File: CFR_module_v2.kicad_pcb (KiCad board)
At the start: 4 copper layers, 80.9 x 70.9 mm, 67 parts, among them J3 Conn_01x02, J4 Conn_01x02, J5 Conn_01x02, Q1 NPN

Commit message: placement des empreintes début
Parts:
- moved D11 37.2 mm to (27.0, 138.7)
- moved R5 37.2 mm to (27.0, 143.3)
- moved C2 36.5 mm to (58.0, 127.5)
- moved ALM1 35.1 mm to (114.0, 130.5)
- moved ALM2 35.1 mm to (97.0, 130.0)
- moved C3 34.2 mm to (56.5, 146.5)
- moved JP1 9.70 mm to (54.5, 65.6), turned to -90 degrees
- moved JP2 7.19 mm to (54.5, 62.0), turned to -90 degrees
- moved R6 1.28 mm to (126.0, 54.5)
- moved C4 0.90 mm to (51.5, 71.0)

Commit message: tout connecté
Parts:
- removed ALM1, ALM2, ALM3: Conn_01x02, Connector_AMASS:AMASS_XT30U-F_1x02_P5.0mm_Vertical
- removed D10, D11, D12: D_Schottky, Diode_SMD:D_SOD-123
- added ALM0: Conn_02x03_Odd_Even, Connector_Molex:Molex_Mini-Fit_Jr_5569-06A2_2x03_P4.20mm_Horizontal, F.Cu at (110.3, 136.8)
- added JP15: Jumper_3_Bridged12, Connector_PinHeader_2.54mm:PinHeader_1x03_P2.54mm_Vertical, F.Cu at (82.8, 86.5)
- added JP16: Jumper_3_Bridged12, Connector_PinHeader_2.54mm:PinHeader_1x03_P2.54mm_Vertical, F.Cu at (82.8, 83.0)
- added JP17: Jumper_3_Bridged12, Connector_PinHeader_2.54mm:PinHeader_1x03_P2.54mm_Vertical, F.Cu at (82.8, 108.5)
- added JP18: Jumper_3_Bridged12, Connector_PinHeader_2.54mm:PinHeader_1x03_P2.54mm_Vertical, F.Cu at (82.8, 105.0)
- added JP19: Jumper_3_Bridged12, Connector_PinHeader_2.54mm:PinHeader_1x03_P2.54mm_Vertical, F.Cu at (82.8, 130.5)
- added JP20: Jumper_3_Bridged12, Connector_PinHeader_2.54mm:PinHeader_1x03_P2.54mm_Vertical, F.Cu at (82.8, 127.0)
- added R4: 10k, Resistor_SMD:R_0805_2012Metric_Pad1.20x1.40mm_HandSolder, B.Cu at (104.5, 87.0)
- BAU1, DBG1, J3, J4, J5: footprint Connector_PinHeader_2.54mm:PinHeader_1x02_P2.54mm_Vertical -> Connector_JST:JST_XH_S2B-XH-A_1x02_P2.50mm_Horizontal
- IO1, IO2: footprint Connector_JST:JST_PH_B4B-PH-K_1x04_P2.00mm_Vertical -> Connector_JST:JST_XH_S4B-XH-A_1x04_P2.50mm_Horizontal
- IO3, IO4, IO5: footprint Connector_JST:JST_PH_B3B-PH-K_1x03_P2.00mm_Vertical -> Connector_JST:JST_XH_S3B-XH-A_1x03_P2.50mm_Horizontal
- MOT1, MOT2, MOT3: value Conn_01x04 -> Conn_02x04_Odd_Even; footprint Connector_PinHeader_2.54mm:PinHeader_1x04_P2.54mm_Vertical -> Connector_PinHeader_2.54mm:PinHeader_2x04_P2.54mm_Horizontal
- R3: value 10k -> 1k
- R5: renamed from R4; value 1k -> 10k
- R6: renamed from R5; value 1k -> 10k
- R7: renamed from R6; value 1k -> 10k
- moved MOT3 128.3 mm to (75.2, 125.6), turned to 180 degrees
- moved C6 123.4 mm to (72.0, 131.1), turned to 180 degrees
- moved DR3 118.1 mm to (78.5, 115.5), turned to 0 degrees
- moved R2 103.5 mm to (123.0, 138.5), turned to 180 degrees
- moved JP5 102.0 mm to (82.8, 122.5), turned to 90 degrees
- moved JP6 98.5 mm to (82.8, 119.0), turned to 90 degrees
- moved BAU1 88.2 mm to (125.0, 141.6), turned to 0 degrees
- moved D9 77.5 mm to (95.5, 120.5), turned to 90 degrees
- moved R6 66.1 mm to (86.0, 113.5), turned to 90 degrees
- moved R7 64.8 mm to (113.0, 118.0), turned to 180 degrees
- moved D8 62.3 mm to (94.5, 113.0)
- moved IO2 58.2 mm to (127.6, 119.5)
- moved D2 58.1 mm to (124.9, 117.5)
- moved IO3 58.1 mm to (127.6, 105.8), turned to 90 degrees
- moved JP8 57.9 mm to (122.3, 115.5)
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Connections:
- net GP0 renamed Net-(DBG1-Pin_2)
- net GP1 renamed Net-(DBG1-Pin_1)
- net GP10 renamed M1_EN_GPIO
- net GP11 renamed M2_IA1_DIR
- net GP12 renamed M2_IA2_STEP
- net GP13 renamed M2_IB1
- net GP14 renamed M2_IB2
- net GP15 renamed M2_EN_GPIO
- net GP16 renamed IO_B1
- net GP17 renamed IO_B2
- net GP18 renamed M3_IA1_DIR
- net GP19 renamed M3_IA2_STEP
- net GP2 renamed IO_A1
- net GP20 renamed M3_IB1
- net GP21 renamed M3_IB2
- net GP22 renamed M3_EN_GPIO
- net GP26_A0 renamed IO_C
- net GP27_A1 renamed IO_D
- net GP28_A2 renamed IO_E
- net GP3 renamed IO_A2
- net GP4 renamed Net-(PiPico0-GPIO4)
- net GP5 renamed M_UART
- net GP6 renamed M1_IA1_DIR
- net GP7 renamed M1_IA2_STEP
- net GP8 renamed M1_IB1
- net GP9 renamed M1_IB2
- D6 pad 2: +5V_Pico -> +5V
- DR1 pad 10: GND -> M1_MS1
- DR1 pad 11: GND -> M1_MS2
- DR2 pad 10: GND -> M2_MS1
- DR2 pad 11: +3V3_Pico -> M2_MS2
- DR3 pad 10: +3V3_Pico -> M3_MS1
- DR3 pad 11: GND -> M3_MS2
- F1 pad 1: +BATT -> VBatt_in
- F1 pad 2: Net-(ALM1-Pin_2) -> +BATT
- F2 pad 2: Net-(ALM2-Pin_2) -> V0_in
- F3 pad 2: Net-(ALM3-Pin_2) -> 5V_in
- JP12 pad 3: +5V_Pico -> +5V
- MOT1 pad 2: Net-(DR1-OA2) -> GND
- MOT1 pad 3: Net-(DR1-OB2) -> Net-(DR1-OA2)
- MOT1 pad 4: Net-(DR1-OB1) -> GND
- MOT2 pad 2: Net-(DR2-OA2) -> GND
- MOT2 pad 3: Net-(DR2-OB2) -> Net-(DR2-OA2)
- MOT2 pad 4: Net-(DR2-OB1) -> GND
- MOT3 pad 2: Net-(DR3-OA2) -> GND
- MOT3 pad 3: Net-(DR3-OB2) -> Net-(DR3-OA2)
- MOT3 pad 4: Net-(DR3-OB1) -> GND
- PiPico0 pad 30: RUN -> unconnected-(PiPico0-RUN-Pad30)
- PiPico0 pad 33: AGND -> unconnected-(PiPico0-AGND-Pad33)
- PiPico0 pad 35: ADC_VREF -> unconnected-(PiPico0-ADC_VREF-Pad35)
- PiPico0 pad 37: 3V3_EN -> unconnected-(PiPico0-3V3_EN-Pad37)
- PiPico0 pad 40: VBUS -> unconnected-(PiPico0-VBUS-Pad40)
- Q1 pad 1: Net-(D7-A) -> Net-(Q1-C)
- R3 pad 2: Net-(D7-A) -> Net-(Q1-C)
- R5 pad 2: Net-(D10-A) -> M1_EN
- R6 pad 2: Net-(D11-A) -> M2_EN
- R7 pad 2: Net-(D12-A) -> M3_EN
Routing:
- net +3V3_Pico: track 0.00 -> 150.6 mm, vias 0 -> 1
- net M_UART: track 0.00 -> 82.9 mm, vias 0 -> 1
- net IO_A1: track 0.00 -> 68.0 mm, vias 0 -> 1
- net IO_A2: track 0.00 -> 64.4 mm, vias 0 -> 1
- net Net-(Q1-B): track 0.00 -> 64.1 mm, vias 0 -> 2
- net M3_IB2: track 0.00 -> 60.6 mm
- net M3_IB1: track 0.00 -> 56.1 mm
- net GND: track 0.00 -> 52.5 mm, vias 0 -> 30
- net M3_IA2_STEP: track 0.00 -> 42.6 mm
- net Net-(D7-A): track 0.00 -> 36.2 mm
- net M3_IA1_DIR: track 0.00 -> 31.2 mm
- net M3_EN: track 0.00 -> 31.1 mm
- net +5V: track 0.00 -> 30.8 mm, vias 0 -> 2
- net M1_IB1: track 0.00 -> 30.0 mm
- net Net-(DBG1-Pin_2): track 0.00 -> 29.7 mm
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- added copper zone on In2.Cu, net +5V
- added copper zone on In2.Cu, net +BATT
- added copper zone on In2.Cu, net +V0
- added copper zone on In2.Cu, net +V1
- added copper zone on In2.Cu, net +V2
- added copper zone on In1.Cu, net GND
- added copper zone on In2.Cu, net VBatt_in
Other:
- board size 80.9 x 70.9 mm -> 72.9 x 88.5 mm
- board text added: "(I2C0,UART0)"
- board text added: "+Batt"
- board text added: "10k"
- board text added: "1k"
- board text added: "EN 10 B1 8 B2 9 A1 DR 6 A2 SP 7 UART 5"
- board text added: "EN 15 B1 13 B2 14 A1-DR 11 A2-SP 12 UART 5"
- board text added: "EN 22 B1 20 B2 21 A1-DR 18 A2-SP 19 UART 5"
- board text added: "IB1"
- board text added: "IB12"
- board text added: "IO1"
- board text added: "IO2"
- board text added: "IO3"
- board text added: "IO4"
- board text added: "IO5"
- board text added: "MS1"
- board text added: "MS2"
- board text removed: "(I2C0, UART0)"
- board text removed: "(Pico)"
- board text removed: "EN: GP10 IB1: GP8 IB2: GP9 IA1-DIR: GP6 IA2-STEP: GP7 UART: GP5"
- board text removed: "EN: GP15 IB1: GP13 IB2: GP14 IA1-DIR: GP11 IA2-STEP: GP12 UART: GP5"
- board text removed: "EN: GP22 IB1: GP20 IB2: GP21 IA1-DIR: GP18 IA2-STEP: GP19 UART: GP5"
- board text removed: "RX/GP1"
- board text removed: "TX/GP0"
- board text removed: "VI"

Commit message: v2 finalisé
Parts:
- removed F1, F2, F3: Fuse, Fuse:Fuse_1206_3216Metric_Pad1.42x1.75mm_HandSolder
- moved G*** 7.50 mm to (85.5, 59.5)
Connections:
- ALM0 pad 3: VBatt_in -> +BATT
- ALM0 pad 4: 5V_in -> +5V
- ALM0 pad 5: VBatt_in -> +BATT
- ALM0 pad 6: V0_in -> +V0
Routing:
- net +BATT: track 29.5 -> 16.3 mm
- net +5V: track 30.8 -> 19.4 mm, vias 2 -> 3
- net +V0: track 6.95 -> 14.3 mm, vias 2 -> 3
- net VBatt_in: track 7.38 -> 0.00 mm, vias 3 -> 0
- net 5V_in: track 4.63 -> 0.00 mm
- net V0_in: track 3.55 -> 0.00 mm
- removed copper zone on In2.Cu, net VBatt_in
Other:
- board text removed: "+Batt"

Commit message: paufinement
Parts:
- removed the G*** at (85.5, 59.5)
- added G***: LOGO, LOGO, F.Cu at (88.0, 66.2)
- added G***: LOGO, LOGO, F.Cu at (74.8, 66.5)
- C3: footprint Capacitor_SMD:CP_Elec_6.3x5.8 -> Capacitor_SMD:CP_Elec_6.3x7.7
- moved H1 0.50 mm to (68.0, 66.5)
- moved H2 0.50 mm to (134.0, 66.5)
- moved DBG1 0.34 mm to (74.0, 72.9)
- moved MOT1 0.16 mm to (75.2, 87.8)
- renumbered J3 to J1, J5 to J2, J4 to J3
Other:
- board size 72.9 x 88.5 mm -> 73 x 88 mm
- board text added: "x"

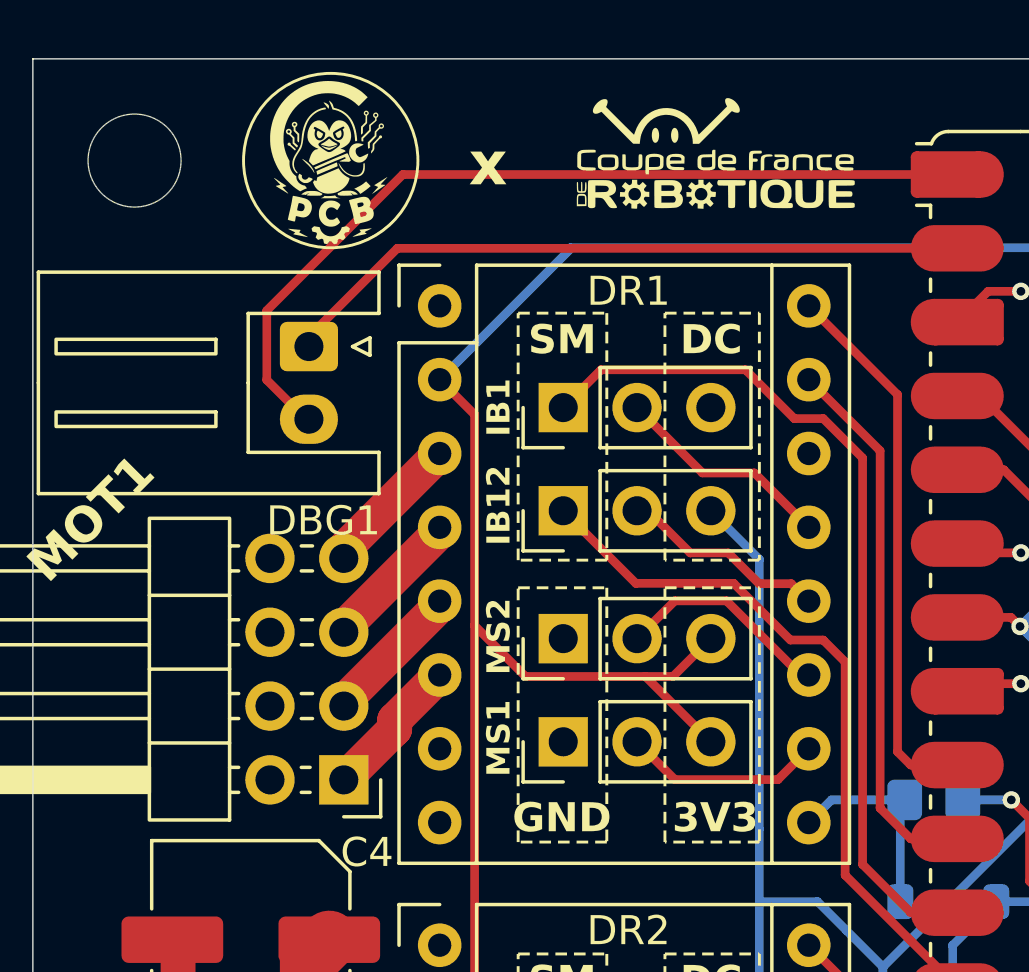
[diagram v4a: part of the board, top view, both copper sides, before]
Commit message: correction erreurs DRC
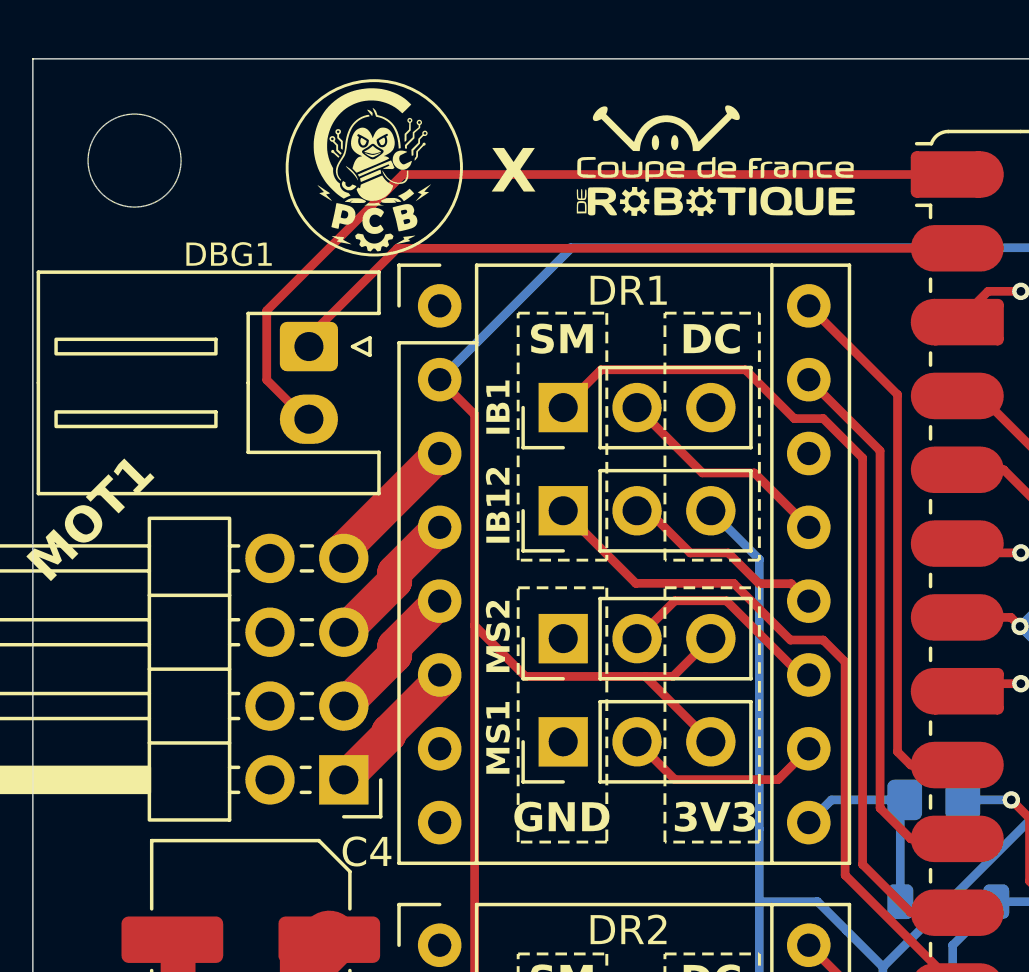
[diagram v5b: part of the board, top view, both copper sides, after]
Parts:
- moved G*** 1.52 mm to (76.2, 66.8)
- moved G*** 0.25 mm to (88.0, 66.5)
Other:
- board text added: "X"
- board text added: "https://github.com/Pingouin-Centrale-Bot/2026-PCB-Module-4-layers.git"
- board text removed: "x"
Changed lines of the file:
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@@
 	(footprint "LOGO"
 		(layer "F.Cu")
-		(at 88 66.25)
+		(at 88 66.5)
 		(property "Reference" "G***"
 			(at 0 0 0)
@@
 	(footprint "LOGO"
 		(layer "F.Cu")
-		(at 74.75 66.5)
+		(at 76.25 66.75)
 		(property "Reference" "G***"
 			(at 0 0 0)
@@
 		(fp_circle
 			(center 0 0)
-			(end 3.35 0)
+			(end 3.45 0)
 			(stroke
 				(width 0.05)
@@
 		(tags "connector JST XH horizontal")
 		(property "Reference" "DBG1"
-			(at 6 -0.5 0)
+			(at -3.15 2.75 0)
 			(layer "F.SilkS")
 			(effects
 				(font
-					(size 1 1)
+					(size 0.8 0.8)
 					(thickness 0.15)
 				)
@@
 		)
 	)
-	(gr_text "x"
-		(at 79.5 67.5 0)
+	(gr_text "X"
+		(at 80.25 67.75 0)
 		(layer "F.SilkS")
 		(effects
@@
 		)
 	)
+	(gr_text "https://github.com/Pingouin-Centrale-Bot/2026-PCB-Module-4-layers.git"
+		(at 101.75 148.5 0)
+		(layer "B.SilkS")
+		(effects
+			(font
+				(size 0.8 0.8)
+				(thickness 0.15)
+				(bold yes)
+			)
+			(justify mirror)
+		)
+	)
 	(gr_text "IO4"
 		(at 134 91.75 90)
@@
 	)
 	(segment
-		(start 75.2 85.11)
-		(end 78.5 81.81)
+		(start 76.951 83.519)
+		(end 75.2 85.27)
+		(width 1.2)
+		(layer "F.Cu")
+		(net 13)
+	)
+	(segment
+		(start 76.951 83.209)
+		(end 76.951 83.519)
 		(width 1.2)
 		(layer "F.Cu")
@@
 	)
 	(segment
-		(start 78.5 81.81)
-		(end 78.5 81.66)
+		(start 78.5 81.66)
+		(end 76.951 83.209)
 		(width 1.2)
 		(layer "F.Cu")
@@
 	)
 	(segment
-		(start 78.5 79.270001)
-		(end 78.5 79.12)
+		(start 76.951 80.979)
+		(end 75.2 82.73)
 		(width 1.2)
 		(layer "F.Cu")
@@
 	)
 	(segment
-		(start 75.2 82.570001)
-		(end 78.5 79.270001)
+		(start 78.5 79.12)
+		(end 76.951 80.669)
 		(width 1.2)
 		(layer "F.Cu")
@@
 	)
 	(segment
-		(start 76.951 85.749)
-		(end 76.951 86.059)
+		(start 76.951 80.669)
+		(end 76.951 80.979)
 		(width 1.2)
 		(layer "F.Cu")
-		(net 16)
+		(net 14)
 	)
 	(segment
-		(start 76.951 86.059)
+		(start 76.75 86.26)
 		(end 75.2 87.81)
 		(width 1.2)
@@
 	)
 	(segment
+		(start 78.5 84.405133)
+		(end 76.75 86.155133)
+		(width 1.2)
+		(layer "F.Cu")
+		(net 16)
+	)
+	(segment
 		(start 78.5 84.2)
-		(end 76.951 85.749)
+		(end 78.5 84.405133)
+		(width 1.2)
+		(layer "F.Cu")
+		(net 16)
+	)
+	(segment
+		(start 76.75 86.155133)
+		(end 76.75 86.26)
 		(width 1.2)
 		(layer "F.Cu")
